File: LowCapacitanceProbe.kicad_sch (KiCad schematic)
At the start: 38 parts, among them J1 u.Fl, J2 u.FL, Q1 BF998, U1 SPX3819M5-L

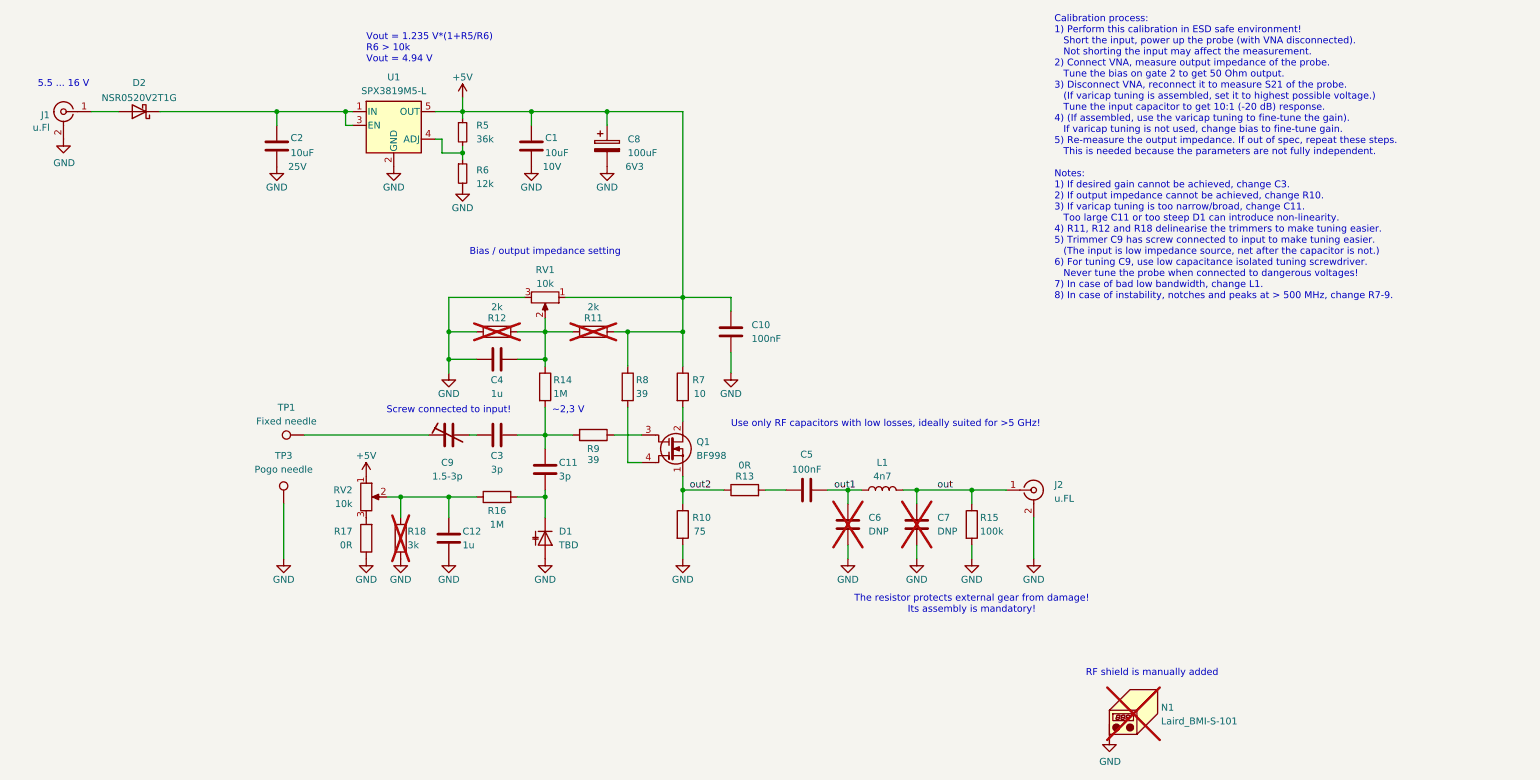
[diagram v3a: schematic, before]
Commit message: Added footprints to all components, added MPNs and Mouser numbers to critical components. Added some notes.
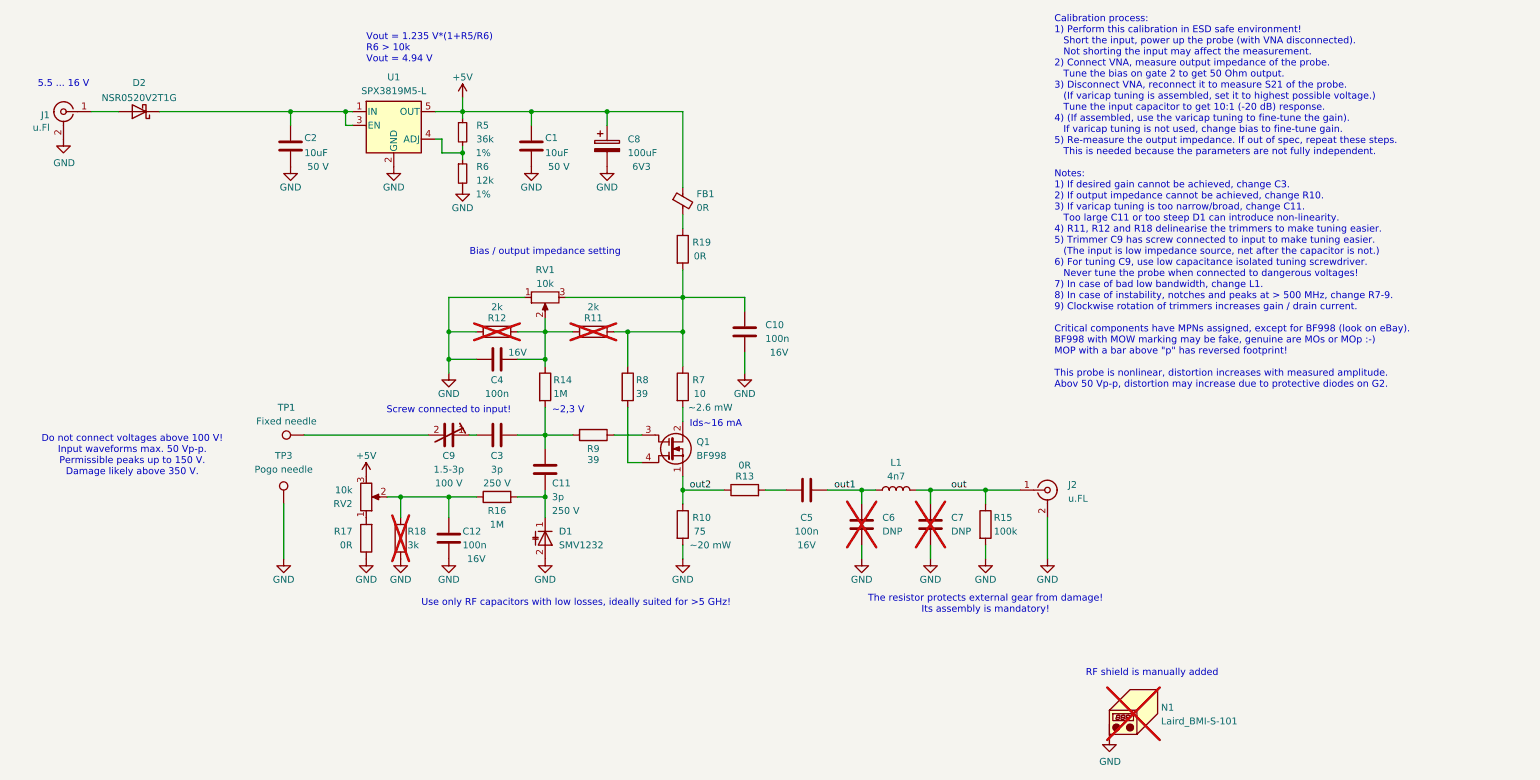
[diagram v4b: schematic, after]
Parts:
- added FB1: 0R, Inductor_SMD:L_0603_1608Metric_Pad1.05x0.95mm_HandSolder, symbol Device:FerriteBead_Small
- added R19: 0R, Resistor_SMD:R_0603_1608Metric_Pad0.98x0.95mm_HandSolder, symbol Device:R
- C1: footprint Capacitor_SMD:C_0402_1005Metric -> Capacitor_SMD:C_1206_3216Metric; LCSC Part C77000 -> (none); MPN GRM155R61A106ME44D -> CL31A106MBHNNNE; Mouser (none) -> 187-CL31A106MBHNNNE; OC_LCSC C77000 -> (none); voltage 10V -> 50 V
- C10, C5: value 100nF -> 100n; footprint Capacitor_SMD:C_1206_3216Metric -> Capacitor_SMD:C_0402_1005Metric_Pad0.74x0.62mm_HandSolder; LCSC Part C2981728 -> (none); LCSC alternative C2981728 -> (none); MPN GRM3195C1H104GA05D -> 530L104KT16T; Mouser (none) -> 581-530L104KT16T; OC_LCSC C907944 -> (none); Rating (none) -> 16V; dielectric NP0 -> (none)
- C11, C3: footprint (none) -> Capacitor_SMD:C_0402_1005Metric_Pad0.74x0.62mm_HandSolder; MPN (none) -> 600F3R0CT250XT; Mouser (none) -> 581-600F3R0CT; Rating (none) -> 250 V
- C12, C4: value 1u -> 100n; footprint (none) -> Capacitor_SMD:C_0402_1005Metric_Pad0.74x0.62mm_HandSolder; MPN (none) -> 530L104KT16T; Mouser (none) -> 581-530L104KT16T; Rating (none) -> 16V
- C2: footprint Capacitor_SMD:C_0603_1608Metric -> Capacitor_SMD:C_1206_3216Metric; LCSC Part C96446 -> (none); MPN CL10A106MA8NRNC -> CL31A106MBHNNNE; Mouser (none) -> 187-CL31A106MBHNNNE; OC_LCSC C96446 -> (none); voltage 25V -> 50 V
- C6, C7: footprint (none) -> Capacitor_SMD:C_0402_1005Metric_Pad0.74x0.62mm_HandSolder
- C8: LCSC Part C2158564 -> (none); Mouser (none) -> 74-T55A107M6R3C0045; OC_LCSC C2158564 -> (none)
- C9: footprint (none) -> Capacitor_SMD:C_Trimmer_Voltronics_JR; MPN (none) -> JR030; Mouser (none) -> 768-JR030; Rating (none) -> 100 V
- D1: value TBD -> SMV1232; footprint (none) -> Diode_SMD:D_SOD-523; MPN (none) -> SMV1231-079LF; Mouser (none) -> 873-SMV1231-079LF
- L1: footprint (none) -> Inductor_SMD:L_0402_1005Metric_Pad0.77x0.64mm_HandSolder; MPN (none) -> LQG15HS4N7B02D; Mouser (none) -> 81-LQG15HS4N7B02D
- R10: footprint (none) -> Resistor_SMD:R_0603_1608Metric_Pad0.98x0.95mm_HandSolder; Rating (none) -> ~20 mW
- R11, R12, R14, R16, R17, R18: footprint (none) -> Resistor_SMD:R_0603_1608Metric_Pad0.98x0.95mm_HandSolder
- R13, R15, R8, R9: footprint (none) -> Resistor_SMD:R_0402_1005Metric_Pad0.72x0.64mm_HandSolder
- R5: footprint Resistor_SMD:R_0402_1005Metric -> Resistor_SMD:R_0603_1608Metric_Pad0.98x0.95mm_HandSolder; LCSC Part C138022 -> (none); MPN RC0402FR-0727KL -> (none); OC_LCSC C138022 -> (none); Tolerance (none) -> 1%; comment general purpose -> (none); dielectric 1% -> (none)
- R6: footprint Resistor_SMD:R_0402_1005Metric -> Resistor_SMD:R_0603_1608Metric_Pad0.98x0.95mm_HandSolder; LCSC Part C114760 -> (none); LCSC alternative C413095 -> (none); MPN RC0402FR-0712KL -> (none); OC_LCSC C114760 -> (none); Tolerance (none) -> 1%; comment general purpose -> (none); dielectric 1% -> (none)
- R7: footprint (none) -> Resistor_SMD:R_0402_1005Metric_Pad0.72x0.64mm_HandSolder; Rating (none) -> ~2.6 mW
- RV1, RV2: footprint (none) -> Potentiometer_THT:Potentiometer_Bourns_3006W_Horizontal; MPN (none) -> Bourns 3006W-1-103; Mouser (none) -> 652-3006W-1-103
- TP1: footprint (none) -> Connector_PinHeader_1.00mm:PinHeader_1x01_P1.00mm_Horizontal; now left out of the parts list
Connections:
- net +5V: now also RV2.3, FB1.1; no longer C10.2, R11.2, R7.1, R8.1, RV1.1, RV2.1
- net GND: now also C12.1, RV1.1; no longer C12.2, RV1.3
- net out1: now also C5.1; no longer C5.2
- net at R13.2: now also C5.2; no longer C5.1
- net at R16.1, R18.2, RV2.2: now also C12.2; no longer C12.1
- net at C3.1: now also C9.1; no longer C9.2
- net at TP1.1: now also C9.2; no longer C9.1
- net at R17.2: now also RV2.1; no longer RV2.3
- new net: FB1.2, R19.1
- new net: C10.2, R11.2, R19.2, R7.1, R8.1, RV1.3
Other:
- note added: "Do not connect voltages above 100 V! Input waveforms max. 50 Vp-p. Permissible peaks up to 150 V. Damage likely above 350 V."
- note added: "Ids~16 mA"
- moved on the sheet: C2, C6, C7, J2, L1, R15

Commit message: refresh after save
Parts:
- removed N1: Laird_BMI-S-101, RF_Shielding:Laird_Technologies_BMI-S-101_13.66x12.70mm, symbol Mechanical:Housing_Pad
- U1: LCSC Part C9056 -> (none); Mouser (none) -> 701-SPX3819M5-L/TR; OC_LCSC C9056 -> (none)
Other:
- note removed: "RF shield is manually added"
- moved on the sheet: C1, C10, C11, C12, C2, C3, C4, C5, C6, C7, C8, C9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

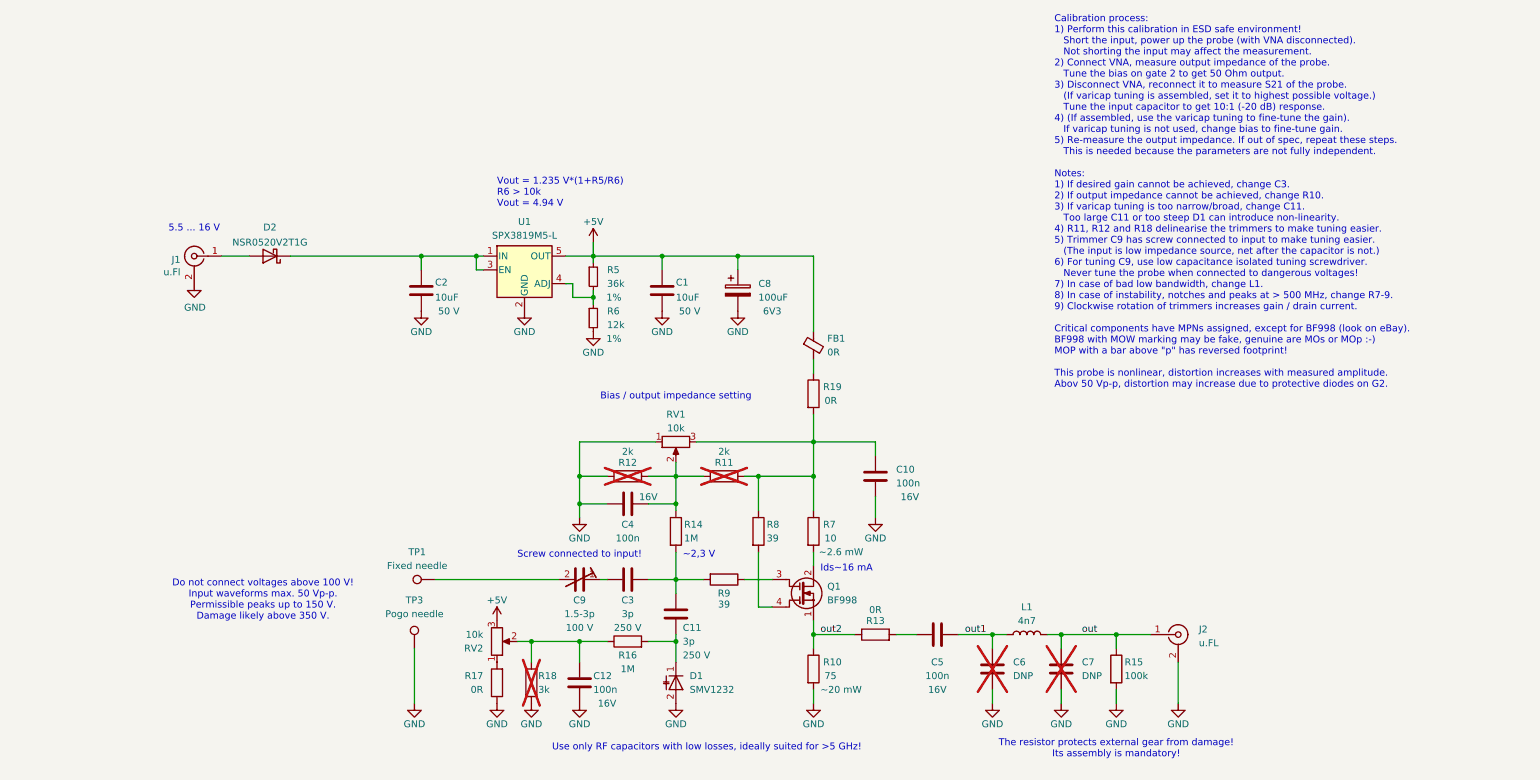
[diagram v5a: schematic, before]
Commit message: Changed output connector to SMA, changed diode for more common one.
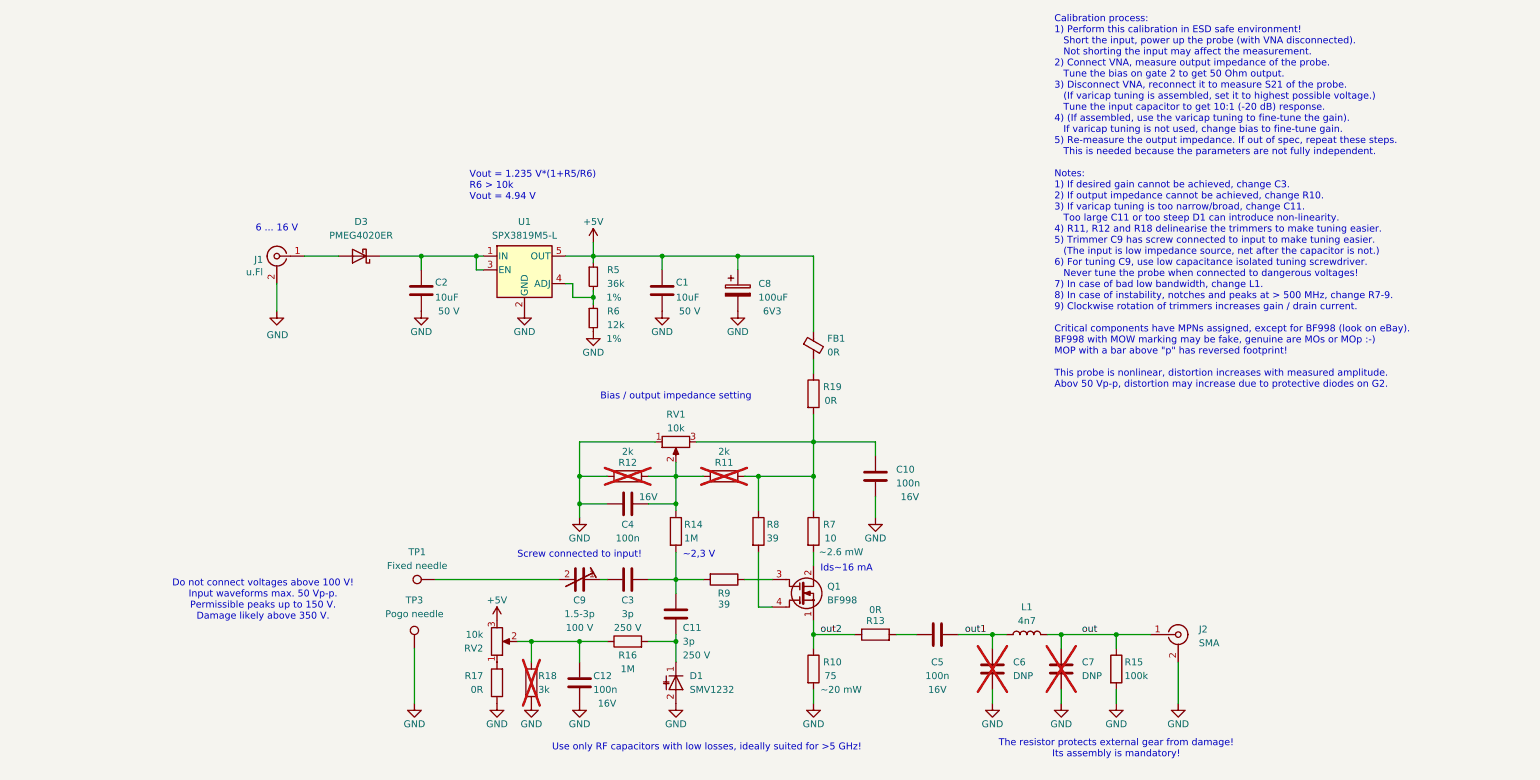
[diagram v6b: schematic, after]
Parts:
- removed D2: NSR0520V2T1G, Diode_SMD:D_SOD-523, symbol Device:D_Schottky
- added D3: PMEG4020ER, Diode_SMD:Nexperia_CFP3_SOD-123W, symbol Diode:PMEG4020ER
- J2: value u.FL -> SMA; footprint Connector_Coaxial:U.FL_Molex_MCRF_73412-0110_Vertical -> Connector_Coaxial:SMA_Amphenol_132289_EdgeMount; MPN (none) -> 132289; Mouser (none) -> 523-132289
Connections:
- net at C2.2, U1.1 (IN), U1.3 (EN): now also D3.1 (K)
- net at J1.1 (In): now also D3.2 (A)
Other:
- note added: "6 ... 16 V"
- note removed: "5.5 ... 16 V"
- moved on the sheet: J1
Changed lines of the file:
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@@
 	(text "Vout = 1.235 V*(1+R5/R6)\nR6 > 10k\nVout = 4.94 V"
 		(exclude_from_sim no)
-		(at 106.68 49.53 0)
+		(at 101.6 48.26 0)
 		(effects
 			(font
@@
 		)
 	)
-	(text "5.5 ... 16 V"
+	(text "6 ... 16 V"
 		(exclude_from_sim no)
-		(at 50.8 53.34 0)
+		(at 66.04 53.34 0)
 		(effects
 			(font
@@
 	(wire
 		(pts
-			(xy 68.58 58.42) (xy 92.71 58.42)
+			(xy 85.09 58.42) (xy 92.71 58.42)
 		)
 		(stroke
@@
 	(wire
 		(pts
+			(xy 66.04 68.58) (xy 66.04 63.5)
+		)
+		(stroke
+			(width 0)
+			(type default)
+		)
+	)
+	(wire
+		(pts
 			(xy 124.46 64.77) (xy 124.46 66.04)
 		)
@@
 	(wire
 		(pts
-			(xy 55.88 58.42) (xy 60.96 58.42)
+			(xy 71.12 58.42) (xy 77.47 58.42)
 		)
 		(stroke
@@
 	(symbol
 		(lib_id "Connector:Conn_Coaxial")
-		(at 50.8 58.42 0)
+		(at 66.04 58.42 0)
 		(mirror y)
 		(unit 1)
@@
 		(dnp no)
 		(property "Reference" "J1"
-			(at 48.26 59.055 0)
+			(at 63.5 59.055 0)
 			(effects
 				(font
@@
 		)
 		(property "Value" "u.Fl"
-			(at 48.26 61.3664 0)
+			(at 63.5 61.3664 0)
 			(effects
 				(font
@@
 		)
 		(property "Footprint" "Connector_Coaxial:U.FL_Molex_MCRF_73412-0110_Vertical"
-			(at 50.8 58.42 0)
+			(at 66.04 58.42 0)
 			(effects
 				(font
@@
 		)
 		(property "Datasheet" " ~"
-			(at 50.8 58.42 0)
+			(at 66.04 58.42 0)
 			(effects
 				(font
@@
 		)
 		(property "Description" ""
-			(at 50.8 58.42 0)
+			(at 66.04 58.42 0)
 			(effects
 				(font
@@
 		)
 		(property "MPN" "CONMHF1-SMD-G-T"
-			(at 50.8 58.42 0)
+			(at 66.04 58.42 0)
 			(effects
 				(font
@@
 		)
 		(property "LCSC Part" "C5137195"
-			(at 50.8 58.42 0)
+			(at 66.04 58.42 0)
 			(effects
 				(font
@@
 	)
 	(symbol
+		(lib_id "Diode:PMEG4020ER")
+		(at 81.28 58.42 180)
+		(unit 1)
+		(exclude_from_sim no)
+		(in_bom yes)
+		(on_board yes)
+		(dnp no)
+		(fields_autoplaced yes)
+		(property "Reference" "D3"
+			(at 81.5975 52.07 0)
+			(effects
+				(font
+					(size 1.27 1.27)
+				)
+			)
+		)
+		(property "Value" "PMEG4020ER"
+			(at 81.5975 54.61 0)
+			(effects
+				(font
+					(size 1.27 1.27)
+				)
+			)
+		)
+		(property "Footprint" "Diode_SMD:Nexperia_CFP3_SOD-123W"
+			(at 81.28 53.975 0)
+			(effects
+				(font
+					(size 1.27 1.27)
+				)
+				(hide yes)
+			)
+		)
+		(property "Datasheet" "https://assets.nexperia.com/documents/data-sheet/PMEG4020ER.pdf"
+			(at 81.28 58.42 0)
+			(effects
+				(font
+					(size 1.27 1.27)
+				)
+				(hide yes)
+			)
+		)
+		(property "Description" "40V, 2A low Vf MEGA Schottky barrier rectifier, SOD-123W"
+			(at 81.28 58.42 0)
+			(effects
+				(font
+					(size 1.27 1.27)
+				)
+				(hide yes)
+			)
+		)
+		(property "MPN" "PMEG4020ER,115"
+			(at 81.28 58.42 0)
+			(effects
+				(font
+					(size 1.27 1.27)
+				)
+				(hide yes)
+			)
+		)
+		(property "Mouser" "771-PMEG4020ER115"
+			(at 81.28 58.42 0)
+			(effects
+				(font
+					(size 1.27 1.27)
+				)
+				(hide yes)
+			)
+		)
+		(pin "2"
+		)
+		(pin "1"
+		)
+		(instances
+			(project ""
+				(path "/e63e39d7-6ac0-4ffd-8aa3-1841a4541b55"
+					(reference "D3")
+					(unit 1)
+				)
+			)
+		)
+	)
+	(symbol
 		(lib_id "Regulator_Linear:SPX3819M5-L")
 		(at 111.76 60.96 0)
@@
 	)
 	(symbol
-		(lib_id "Device:D_Schottky")
-		(at 64.77 58.42 180)
-		(unit 1)
-		(exclude_from_sim no)
-		(in_bom yes)
-		(on_board yes)
-		(dnp no)
-		(property "Reference" "D2"
-			(at 64.77 53.1049 0)
-			(effects
-				(font
-					(size 1.27 1.27)
-				)
-			)
-		)
-		(property "Value" "NSR0520V2T1G"
-			(at 64.77 55.88 0)
-			(effects
-				(font
-					(size 1.27 1.27)
-				)
-			)
-		)
-		(property "Footprint" "Diode_SMD:D_SOD-523"
-			(at 64.77 58.42 0)
-			(effects
-				(font
-					(size 1.27 1.27)
-				)
-				(hide yes)
-			)
-		)
-		(property "Datasheet" "~"
-			(at 64.77 58.42 0)
-			(effects
-				(font
-					(size 1.27 1.27)
-				)
-				(hide yes)
-			)
-		)
-		(property "Description" ""
-			(at 64.77 58.42 0)
-			(effects
-				(font
-					(size 1.27 1.27)
-				)
-				(hide yes)
-			)
-		)
-		(property "comment" "just about any schottky will do"
-			(at 64.77 58.42 0)
-			(effects
-				(font
-					(size 1.27 1.27)
-				)
-				(hide yes)
-			)
-		)
-		(property "MPN" "NSR0520V2T1G"
-			(at 64.77 58.42 0)
-			(effects
-				(font
-					(size 1.27 1.27)
-				)
-				(hide yes)
-			)
-		)
-		(property "OC_LCSC" "C99683"
-			(at 64.77 58.42 0)
-			(effects
-				(font
-					(size 1.27 1.27)
-				)
-				(hide yes)
-			)
-		)
-		(property "LCSC Part" "C99683"
-			(at 64.77 58.42 0)
-			(effects
-				(font
-					(size 1.27 1.27)
-				)
-				(hide yes)
-			)
-		)
-		(pin "1"
-		)
-		(pin "2"
-		)
-		(instances
-			(project "FETProbe_v2"
-				(path "/e63e39d7-6ac0-4ffd-8aa3-1841a4541b55"
-					(reference "D2")
-					(unit 1)
-				)
-			)
-		)
-	)
-	(symbol
 		(lib_id "Device:C_Trim")
 		(at 121.92 118.11 270)
@@
 	(symbol
 		(lib_id "power:GND")
-		(at 50.8 63.5 0)
+		(at 66.04 68.58 0)
 		(unit 1)
 		(exclude_from_sim no)
@@
 		(dnp no)
 		(property "Reference" "#PWR01"
-			(at 50.8 69.85 0)
+			(at 66.04 74.93 0)
 			(effects
 				(font
@@
 		)
 		(property "Value" "GND"
-			(at 50.927 67.8942 0)
+			(at 66.167 72.9742 0)
 			(effects
 				(font
@@
 		)
 		(property "Footprint" ""
-			(at 50.8 63.5 0)
+			(at 66.04 68.58 0)
 			(effects
 				(font
@@
 		)
 		(property "Datasheet" ""
-			(at 50.8 63.5 0)
+			(at 66.04 68.58 0)
 			(effects
 				(font
@@
 		)
 		(property "Description" ""
-			(at 50.8 63.5 0)
+			(at 66.04 68.58 0)
 			(effects
 				(font
@@
 			)
 		)
-		(property "Value" "u.FL"
+		(property "Value" "SMA"
 			(at 236.22 129.8331 0)
 			(effects
@@
 			)
 		)
-		(property "Footprint" "Connector_Coaxial:U.FL_Molex_MCRF_73412-0110_Vertical"
+		(property "Footprint" "Connector_Coaxial:SMA_Amphenol_132289_EdgeMount"
 			(at 232.41 128.27 0)
 			(effects
@@
 			)
 		)
-		(property "Datasheet" "~"
+		(property "Datasheet" "https://cz.mouser.com/datasheet/2/18/1/amphs06501_1-2259276.pdf"
 			(at 232.41 128.27 0)
 			(effects
@@
 			(at 232.41 128.27 0)
 			(effects
+				(font
+					(size 1.27 1.27)
+				)
+				(hide yes)
+			)
+		)
+		(property "Mouser" "523-132289"
+			(at 232.41 128.27 0)
+			(effects
+				(font
+					(size 1.27 1.27)
+				)
+				(hide yes)
+			)
+		)
+		(property "MPN" "132289"
+			(at 232.41 128.27 0)
+			(effects
